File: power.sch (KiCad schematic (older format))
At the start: 57 parts, among them J12 Barrel_Jack_Switch, J13 Conn_02x05_Odd_Even, J14 Screw_Terminal_01x12, U13 LT3471, U14 LP38692MP-5.0, U15 LP38693MP-3.3, U16 LM2937xMP, U17 MAX6070BAUT21+T, U18 LP38693MP-1.8, U19 MC79M15_TO252, U20 LP38693MP-2.5

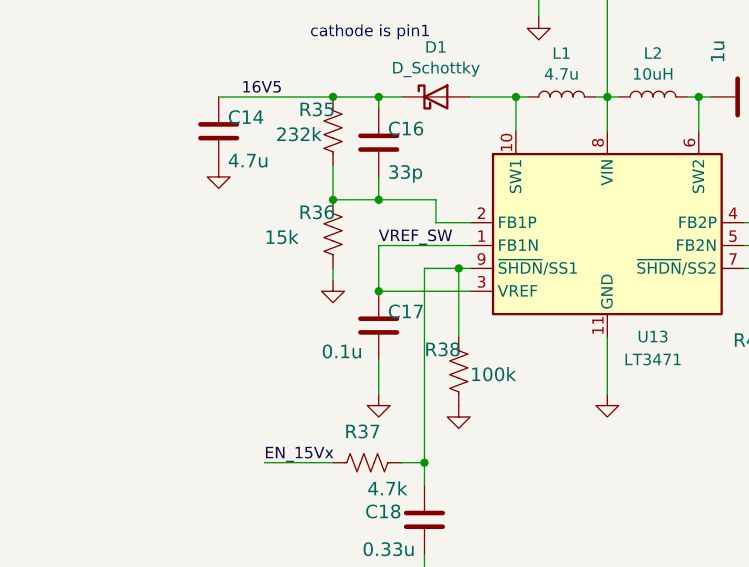
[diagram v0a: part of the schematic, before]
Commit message: added 3d renderings
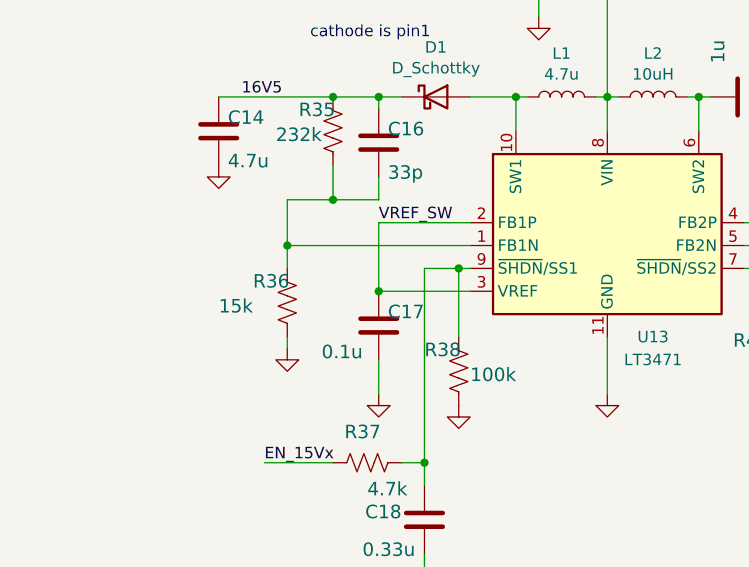
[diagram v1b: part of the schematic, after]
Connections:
- net VREF_SW: now also U13.2 (FB1P); no longer U13.1 (FB1N)
- net at C16.2, R35.2, R36.1: now also U13.1 (FB1N); no longer U13.2 (FB1P)
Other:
- moved on the sheet: R36
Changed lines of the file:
@@
 L Device:R_US R36
 U 1 1 60F53569
-P 1800 4700
-F 0 "R36" H 1650 4759 59  0000 L BNN
-F 1 "15k" H 1500 4650 59  0000 L BNN
-F 2 "Resistor_SMD:R_0603_1608Metric" H 1800 4700 50  0001 C CNN
-F 3 "" H 1800 4700 50  0001 C CNN
-F 4 "RC0603FR-0715kL" H 1650 4859 50  0001 C CNN "Manf#"
-F 5 "0.1W" H 1650 4859 50  0001 C CNN "Power"
-F 6 "1%" H 1650 4859 50  0001 C CNN "Tolerance"
-	1    1800 4700
+P 1600 5000
+F 0 "R36" H 1450 5059 59  0000 L BNN
+F 1 "15k" H 1300 4950 59  0000 L BNN
+F 2 "Resistor_SMD:R_0603_1608Metric" H 1600 5000 50  0001 C CNN
+F 3 "" H 1600 5000 50  0001 C CNN
+F 4 "RC0603FR-0715kL" H 1450 5159 50  0001 C CNN "Manf#"
+F 5 "0.1W" H 1450 5159 50  0001 C CNN "Power"
+F 6 "1%" H 1450 5159 50  0001 C CNN "Tolerance"
+	1    1600 5000
 	1    0    0    -1
 $EndComp
@@
 L power:GND #GND026
 U 1 1 60F758E0
-P 1800 4900
-F 0 "#GND026" H 1800 4900 50  0001 C CNN
-F 1 "GND" H 1700 4800 59  0001 L BNN
-F 2 "" H 1800 4900 50  0001 C CNN
-F 3 "" H 1800 4900 50  0001 C CNN
-	1    1800 4900
+P 1600 5200
+F 0 "#GND026" H 1600 5200 50  0001 C CNN
+F 1 "GND" H 1500 5100 59  0001 L BNN
+F 2 "" H 1600 5200 50  0001 C CNN
+F 3 "" H 1600 5200 50  0001 C CNN
+	1    1600 5200
 	1    0    0    -1
 $EndComp
@@
 Text Label 3000 3350 0    50   ~ 0
 6V_IN
-Text Label 2000 4750 0    50   ~ 0
+Text Label 2000 4650 0    50   ~ 0
 VREF_SW
 Text Label 4350 5100 0    50   ~ 0
@@
 	2400 4100 2600 4100
 Wire Wire Line
-	2400 4750 2000 4750
-Wire Wire Line
-	2000 4750 2000 4950
-Wire Wire Line
 	2000 4950 2400 4950
 Wire Wire Line
-	2250 4550 2250 4650
-Wire Wire Line
-	2250 4650 2400 4650
-Wire Wire Line
-	1800 4900 1800 4850
+	1600 5200 1600 5150
 Wire Wire Line
 	1800 4550 1800 4400
@@
 Wire Wire Line
 	2000 4450 2000 4550
-Wire Wire Line
-	2000 4550 2250 4550
 Wire Wire Line
 	2000 4150 2000 4100
@@
 Connection ~ 6700 2300
 Connection ~ 8850 2300
-Connection ~ 1800 4550
 Connection ~ 3000 4100
 Connection ~ 2600 4100
@@
 Connection ~ 4350 4650
 Connection ~ 4600 4100
-Connection ~ 2000 4550
 Connection ~ 2000 4100
 Connection ~ 3750 4850
@@
 Wire Wire Line
 	11250 4550 11500 4550
+Wire Wire Line
+	1800 4550 1600 4550
+Wire Wire Line
+	1600 4550 1600 4750
+Connection ~ 1800 4550
+Wire Wire Line
+	2000 4650 2000 4950
+Wire Wire Line
+	2000 4650 2400 4650
+Wire Wire Line
+	2400 4750 1600 4750
+Wire Wire Line
+	1600 4850 1600 4750
+Connection ~ 1600 4750
 $EndSCHEMATC

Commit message: DC-DC Regulator updated
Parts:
- C14, C15, C16, C17, C18, C19, C20, C21, C22, C23, C24, C25, C26, C27, C28, C29, C30, C31, C32, C33, C34, C35, C36, C37: symbol Device:C -> covg_daq_v2-rescue:C-Device
- D1, D2: symbol Device:D_Schottky -> covg_daq_v2-rescue:D_Schottky-Device
- FB7: symbol Device:Ferrite_Bead -> covg_daq_v2-rescue:Ferrite_Bead-Device
- J12: symbol Connector:Barrel_Jack_Switch -> covg_daq_v2-rescue:Barrel_Jack_Switch-Connector
- J13: symbol Connector_Generic:Conn_02x05_Odd_Even -> covg_daq_v2-rescue:Conn_02x05_Odd_Even-Connector_Generic
- J14: symbol Connector:Screw_Terminal_01x12 -> covg_daq_v2-rescue:Screw_Terminal_01x12-Connector
- L1: footprint covg-kicad:SRR4018-4R7Y -> Inductor_SMD:L_Bourns-SRN4018; symbol Device:L -> covg_daq_v2-rescue:L-Device; Manf# SRR4018-4R7Y -> SRN4018-4R7M
- L2: footprint covg-kicad:NRS5020T100MMGJ -> Inductor_SMD:L_Bourns-SRN4018; symbol Device:L -> covg_daq_v2-rescue:L-Device; Manf# NRS5020T100MMGJ -> SRN4018-100M
- L3: footprint covg-kicad:SRR6028-150Y -> Inductor_SMD:L_Bourns-SRN4018; symbol Device:L -> covg_daq_v2-rescue:L-Device; Manf# SRR6028-150Y‎ -> SRN4018-150M
- R35, R36, R37, R38, R39, R40, R41, R42, R43, R44, R45: symbol Device:R_US -> covg_daq_v2-rescue:R_US-Device
- R46, R47, R48, R49, R50: symbol Device:R_Small_US -> covg_daq_v2-rescue:R_Small_US-Device
- U13: symbol Regulator_Switching:LT3471 -> covg_daq_v2-rescue:LT3471-Regulator_Switching
- U14: symbol Regulator_Linear:LP38693MP-5.0 -> covg_daq_v2-rescue:LP38693MP-5.0-Regulator_Linear
- U15: symbol Regulator_Linear:LP38693MP-3.3 -> covg_daq_v2-rescue:LP38693MP-3.3-Regulator_Linear
- U16: symbol Regulator_Linear:LM2937xMP -> covg_daq_v2-rescue:LM2937xMP-Regulator_Linear
- U17: symbol covg-kicad:MAX6070BAUT21+T -> covg_daq_v2-rescue:MAX6070BAUT21+T-covg-kicad
- U18: symbol Regulator_Linear:LP38693MP-1.8 -> covg_daq_v2-rescue:LP38693MP-1.8-Regulator_Linear
- U19: symbol Regulator_Linear:MC79M15_TO252 -> covg_daq_v2-rescue:MC79M15_TO252-Regulator_Linear
- U20: symbol Regulator_Linear:LP38693MP-2.5 -> covg_daq_v2-rescue:LP38693MP-2.5-Regulator_Linear

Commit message: rolled back to commit b6c4f66 because of rescue libraries
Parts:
- C14, C15, C16, C17, C18, C19, C20, C21, C22, C23, C24, C25, C26, C27, C28, C29, C30, C31, C32, C33, C34, C35, C36, C37: symbol covg_daq_v2-rescue:C-Device -> Device:C
- D1, D2: symbol covg_daq_v2-rescue:D_Schottky-Device -> Device:D_Schottky
- FB7: symbol covg_daq_v2-rescue:Ferrite_Bead-Device -> Device:Ferrite_Bead
- J12: symbol covg_daq_v2-rescue:Barrel_Jack_Switch-Connector -> Connector:Barrel_Jack_Switch
- J13: symbol covg_daq_v2-rescue:Conn_02x05_Odd_Even-Connector_Generic -> Connector_Generic:Conn_02x05_Odd_Even
- J14: symbol covg_daq_v2-rescue:Screw_Terminal_01x12-Connector -> Connector:Screw_Terminal_01x12
- L1: footprint Inductor_SMD:L_Bourns-SRN4018 -> covg-kicad:SRR4018-4R7Y; symbol covg_daq_v2-rescue:L-Device -> Device:L; Manf# SRN4018-4R7M -> SRR4018-4R7Y
- L2: footprint Inductor_SMD:L_Bourns-SRN4018 -> covg-kicad:NRS5020T100MMGJ; symbol covg_daq_v2-rescue:L-Device -> Device:L; Manf# SRN4018-100M -> NRS5020T100MMGJ
- L3: footprint Inductor_SMD:L_Bourns-SRN4018 -> covg-kicad:SRR6028-150Y; symbol covg_daq_v2-rescue:L-Device -> Device:L; Manf# SRN4018-150M -> SRR6028-150Y‎
- R35, R36, R37, R38, R39, R40, R41, R42, R43, R44, R45: symbol covg_daq_v2-rescue:R_US-Device -> Device:R_US
- R46, R47, R48, R49, R50: symbol covg_daq_v2-rescue:R_Small_US-Device -> Device:R_Small_US
- U13: symbol covg_daq_v2-rescue:LT3471-Regulator_Switching -> Regulator_Switching:LT3471
- U14: symbol covg_daq_v2-rescue:LP38693MP-5.0-Regulator_Linear -> Regulator_Linear:LP38693MP-5.0
- U15: symbol covg_daq_v2-rescue:LP38693MP-3.3-Regulator_Linear -> Regulator_Linear:LP38693MP-3.3
- U16: symbol covg_daq_v2-rescue:LM2937xMP-Regulator_Linear -> Regulator_Linear:LM2937xMP
- U17: symbol covg_daq_v2-rescue:MAX6070BAUT21+T-covg-kicad -> covg-kicad:MAX6070BAUT21+T
- U18: symbol covg_daq_v2-rescue:LP38693MP-1.8-Regulator_Linear -> Regulator_Linear:LP38693MP-1.8
- U19: symbol covg_daq_v2-rescue:MC79M15_TO252-Regulator_Linear -> Regulator_Linear:MC79M15_TO252
- U20: symbol covg_daq_v2-rescue:LP38693MP-2.5-Regulator_Linear -> Regulator_Linear:LP38693MP-2.5

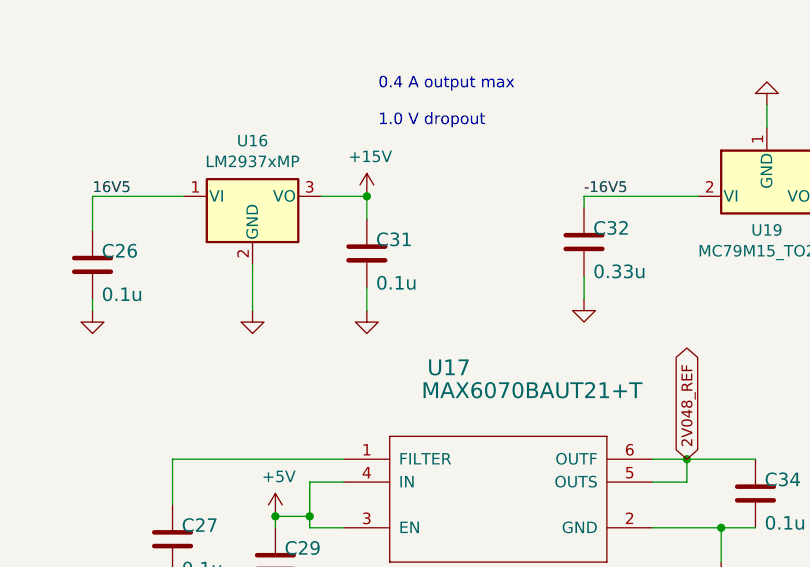
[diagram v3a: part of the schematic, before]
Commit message: move around signals for easier routing
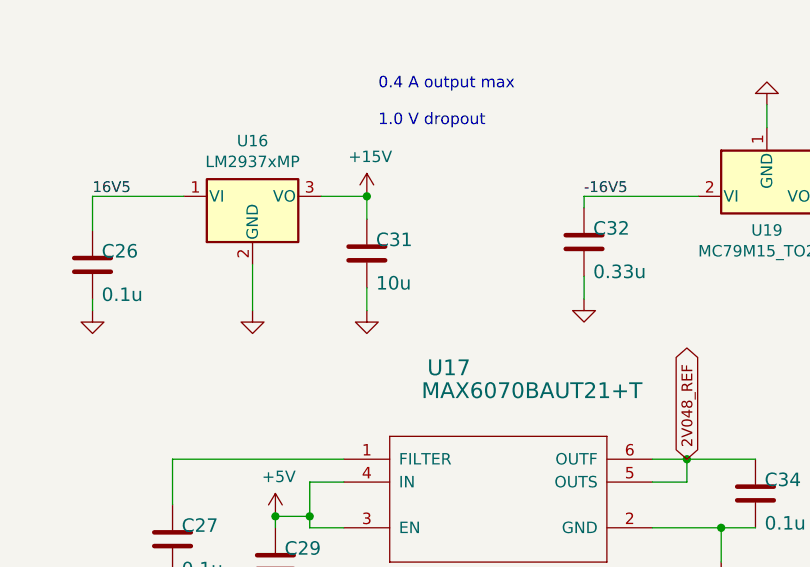
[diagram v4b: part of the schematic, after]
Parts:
- C31: value 0.1u -> 10u; footprint Capacitor_SMD:C_0603_1608Metric -> Capacitor_SMD:C_0805_2012Metric; Manf# CL10B104KA8NFNC -> TMK212BBJ106MG-T; Manufacturer_Name Samsung -> Taiyo Yuden; Tolerance 10% -> 20%
- C35: Manf# CL10B105KO8NNNC -> CL10A105KA8NFNC; voltage 16V -> 25V
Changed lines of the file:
@@
 P 7250 4400
 F 0 "C31" H 7290 4425 59  0000 L BNN
-F 1 "0.1u" H 7290 4235 59  0000 L BNN
-F 2 "Capacitor_SMD:C_0603_1608Metric" H 7250 4400 50  0001 C CNN
+F 1 "10u" H 7290 4235 59  0000 L BNN
+F 2 "Capacitor_SMD:C_0805_2012Metric" H 7250 4400 50  0001 C CNN
 F 3 "" H 7250 4400 50  0001 C CNN
-F 4 "CL10B104KA8NFNC" H 7290 4525 50  0001 C CNN "Manf#"
-F 5 "Samsung" H 7290 4525 50  0001 C CNN "Manufacturer_Name"
-F 6 "10%" H 7290 4525 50  0001 C CNN "Tolerance"
+F 4 "TMK212BBJ106MG-T" H 7290 4525 50  0001 C CNN "Manf#"
+F 5 "Taiyo Yuden" H 7290 4525 50  0001 C CNN "Manufacturer_Name"
+F 6 "20%" H 7290 4525 50  0001 C CNN "Tolerance"
 F 7 "25" H 7290 4525 50  0001 C CNN "voltage"
 	1    7250 4400
@@
 F 2 "Capacitor_SMD:C_0603_1608Metric" H 9550 4350 50  0001 C CNN
 F 3 "" H 9550 4350 50  0001 C CNN
-F 4 "CL10B105KO8NNNC" H 9590 4475 50  0001 C CNN "Manf#"
+F 4 "CL10A105KA8NFNC" H 9590 4475 50  0001 C CNN "Manf#"
 F 5 "10%" H 9590 4475 50  0001 C CNN "Tolerance"
-F 6 "16V" H 9590 4475 50  0001 C CNN "voltage"
+F 6 "25V" H 9590 4475 50  0001 C CNN "voltage"
 	1    9550 4350
 	1    0    0    -1

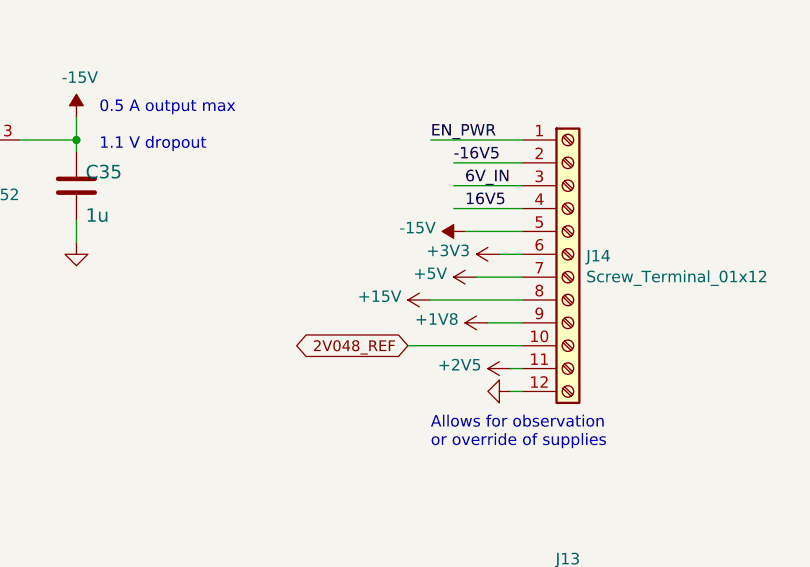
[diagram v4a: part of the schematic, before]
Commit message: reshape power planes
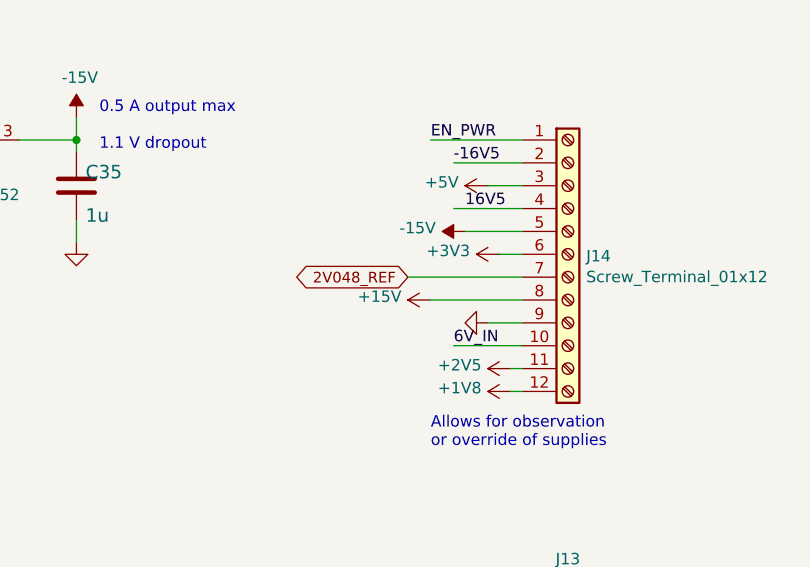
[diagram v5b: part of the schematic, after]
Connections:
- net +1V8: now also J14.12 (Pin_12); no longer J14.9 (Pin_9)
- net +5V: now also J14.3 (Pin_3); no longer J14.7 (Pin_7)
- net 2V048_REF: now also J14.7 (Pin_7); no longer J14.10 (Pin_10)
- net 6V_IN: now also J14.10 (Pin_10); no longer J14.3 (Pin_3)
- net GND: now also J14.9 (Pin_9); no longer J14.12 (Pin_12)
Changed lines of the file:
@@
-$EndComp
-$Comp
-L power:+5V #PWR074
-U 1 1 612190C3
-P 11300 4750
-F 0 "#PWR074" H 11300 4600 50  0001 C CNN
-F 1 "+5V" V 11315 4878 50  0000 L CNN
-F 2 "" H 11300 4750 50  0001 C CNN
-F 3 "" H 11300 4750 50  0001 C CNN
-	1    11300 4750
-	0    -1   -1   0
 $EndComp
 $Comp
@@
 L power:+1V8 #PWR075
 U 1 1 61303020
-P 11350 4950
-F 0 "#PWR075" H 11350 4800 50  0001 C CNN
-F 1 "+1V8" V 11365 5078 50  0000 L CNN
-F 2 "" H 11350 4950 50  0001 C CNN
-F 3 "" H 11350 4950 50  0001 C CNN
-	1    11350 4950
+P 11450 5250
+F 0 "#PWR075" H 11450 5100 50  0001 C CNN
+F 1 "+1V8" V 11465 5378 50  0000 L CNN
+F 2 "" H 11450 5250 50  0001 C CNN
+F 3 "" H 11450 5250 50  0001 C CNN
+	1    11450 5250
 	0    -1   -1   0
 $EndComp
@@
 Text Label 11250 4450 0    50   ~ 0
 16V5
-Text Label 11250 4350 0    50   ~ 0
+Text Label 11200 5050 0    50   ~ 0
 6V_IN
 Text Notes 11100 5500 0    50   ~ 0
@@
 Text HLabel 10450 6500 0    50   Input ~ 0
 EN_15V
-Text GLabel 11000 5050 0    47   BiDi ~ 0
+Text GLabel 11000 4750 0    47   BiDi ~ 0
 2V048_REF
 Text Label 1500 2250 0    47   ~ 0
@@
 	1200 2450 1100 2450
 Wire Wire Line
-	11200 4350 11500 4350
+	11200 5050 11500 5050
 Wire Wire Line
 	11200 4250 11500 4250
 Wire Wire Line
-	11000 5050 11500 5050
+	11000 4750 11500 4750
 Wire Wire Line
 	7000 5400 7000 5550
@@
 Wire Wire Line
 	6400 5300 6400 5500
-Wire Wire Line
-	11300 4750 11500 4750
 Wire Wire Line
 	2700 3750 2700 3650
@@
 L power:GND #GND0280
 U 1 1 60FF305F
-P 11450 5250
-F 0 "#GND0280" H 11450 5250 50  0001 C CNN
-F 1 "GND" H 11350 5150 59  0001 L BNN
-F 2 "" H 11450 5250 50  0001 C CNN
-F 3 "" H 11450 5250 50  0001 C CNN
-	1    11450 5250
+P 11350 4950
+F 0 "#GND0280" H 11350 4950 50  0001 C CNN
+F 1 "GND" H 11250 4850 59  0001 L BNN
+F 2 "" H 11350 4950 50  0001 C CNN
+F 3 "" H 11350 4950 50  0001 C CNN
+	1    11350 4950
 	0    1    1    0
 $EndComp
@@
 	1600 4850 1600 4750
 Connection ~ 1600 4750
+$Comp
+L power:+5V #PWR0285
+U 1 1 61BB6917
+P 11350 4350
+F 0 "#PWR0285" H 11350 4200 50  0001 C CNN
+F 1 "+5V" V 11365 4478 50  0000 L CNN
+F 2 "" H 11350 4350 50  0001 C CNN
+F 3 "" H 11350 4350 50  0001 C CNN
+	1    11350 4350
+	0    -1   -1   0
+$EndComp
+Wire Wire Line
+	11350 4350 11500 4350
 $EndSCHEMATC

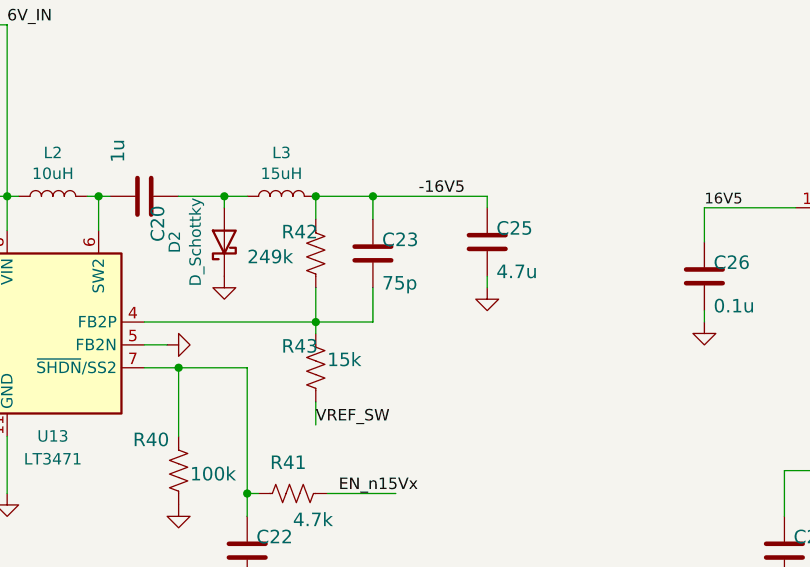
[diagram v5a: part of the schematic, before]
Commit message: updates to power planes
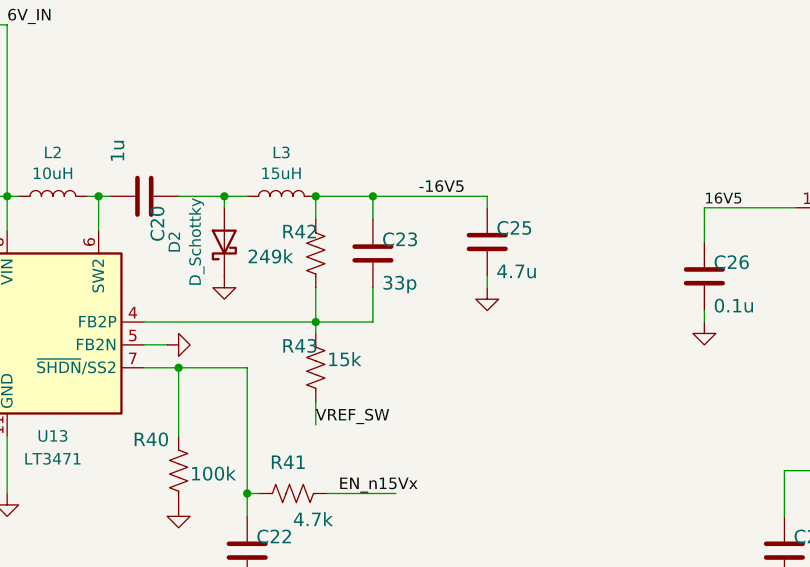
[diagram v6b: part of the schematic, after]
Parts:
- C23: value 75p -> 33p; Manf# CC0603JRNPO9BN750 -> CC0603JRNPO9BN330
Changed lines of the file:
@@
 P 4600 4350
 F 0 "C23" H 4640 4375 59  0000 L BNN
-F 1 "75p" H 4640 4185 59  0000 L BNN
+F 1 "33p" H 4640 4185 59  0000 L BNN
 F 2 "Capacitor_SMD:C_0603_1608Metric" H 4600 4350 50  0001 C CNN
 F 3 "" H 4600 4350 50  0001 C CNN
-F 4 "CC0603JRNPO9BN750" H 4640 4475 50  0001 C CNN "Manf#"
+F 4 "CC0603JRNPO9BN330" H 4640 4475 50  0001 C CNN "Manf#"
 F 5 "5%" H 4640 4475 50  0001 C CNN "Tolerance"
 F 6 "50V" H 4640 4475 50  0001 C CNN "voltage"

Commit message: schematic updates
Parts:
- L3: Manf# SRR6028-150Y‎ -> SRR6028-150Y
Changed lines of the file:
@@
 F 2 "covg-kicad:SRR6028-150Y" H 4200 4100 50  0001 C CNN
 F 3 "~" H 4200 4100 50  0001 C CNN
-F 4 "SRR6028-150Y‎" V 4200 4100 50  0001 C CNN "Manf#"
+F 4 "SRR6028-150Y" V 4200 4100 50  0001 C CNN "Manf#"
 	1    4200 4100
 	0    -1   -1   0
